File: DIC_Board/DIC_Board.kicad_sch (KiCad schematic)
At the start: 0 parts

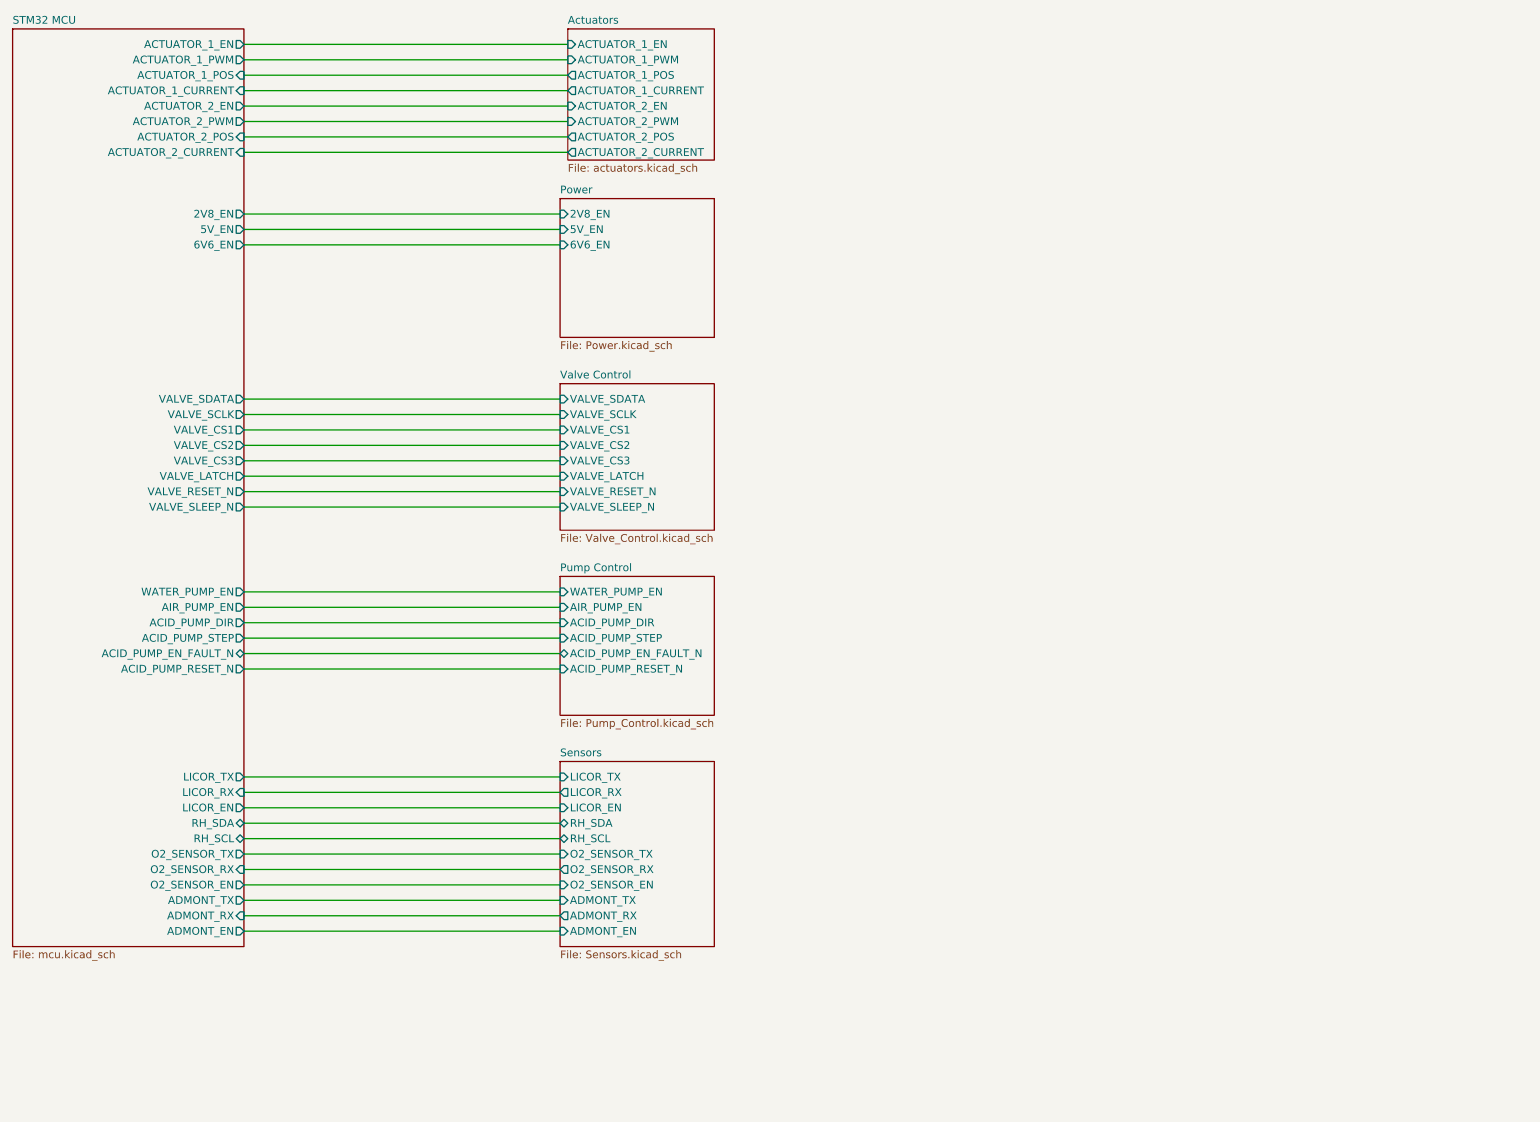
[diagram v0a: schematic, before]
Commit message: Synchronize power, communications, and MCU configuration
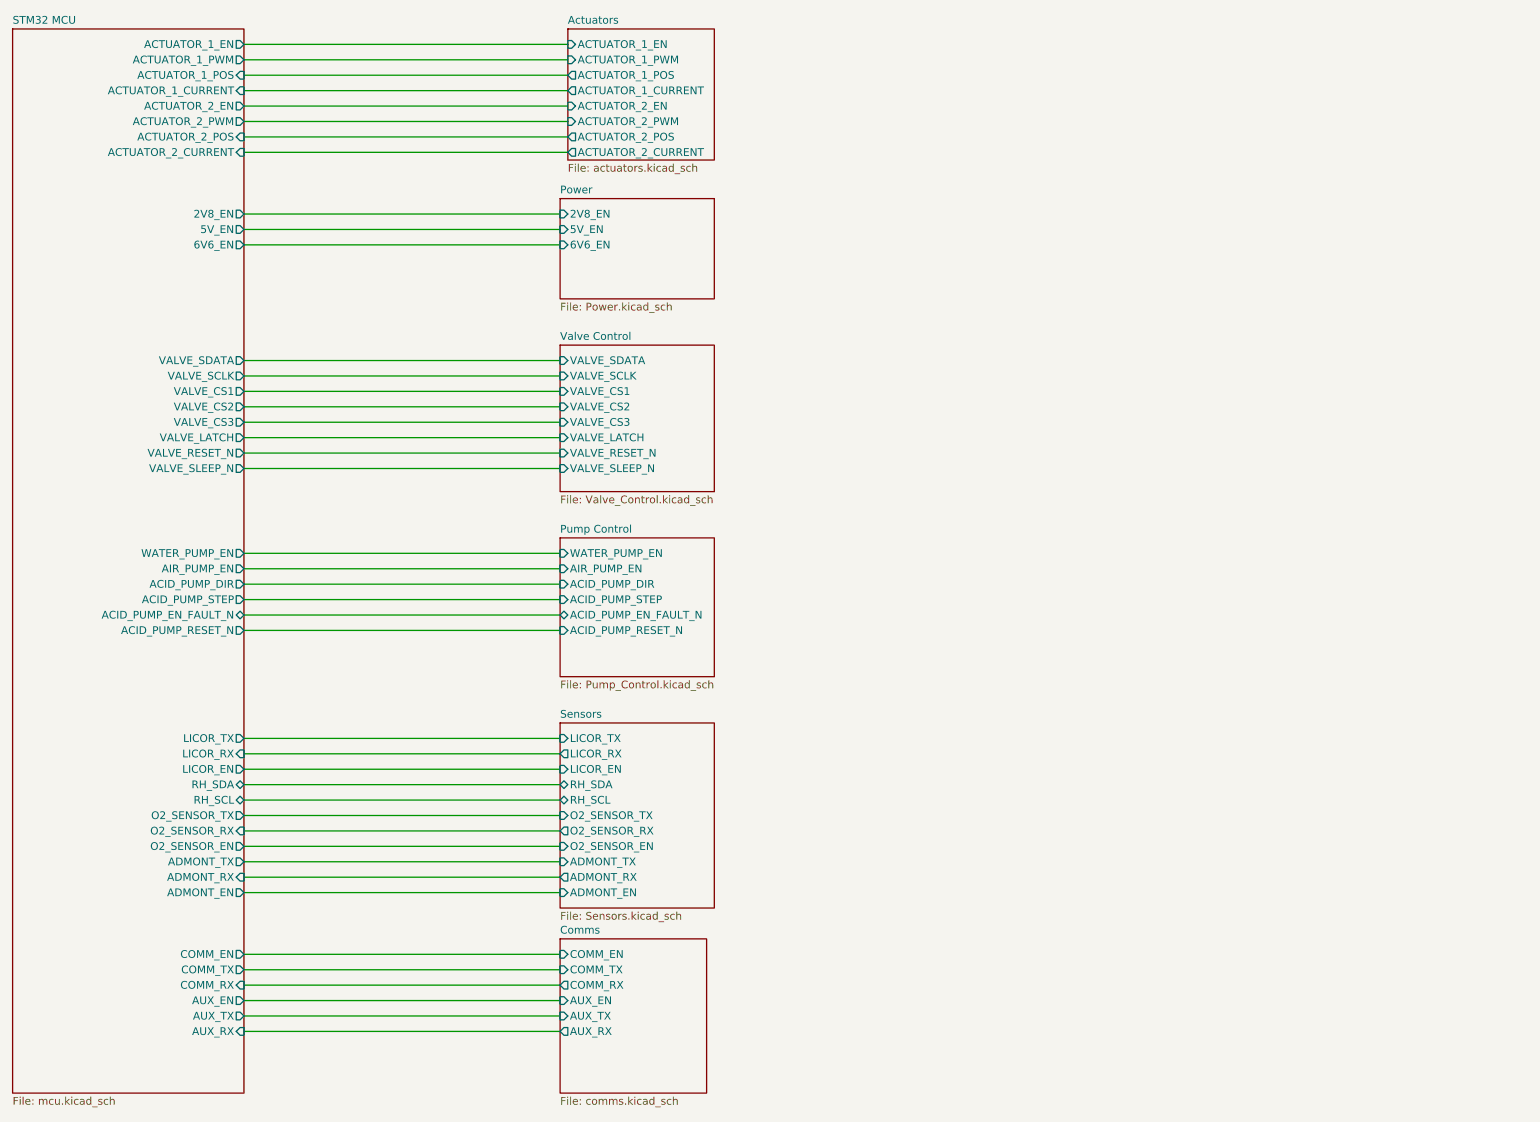
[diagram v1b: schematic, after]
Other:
- added sheet Comms (comms.kicad_sch)
- sheet STM32 MCU ports: added AUX_EN, AUX_RX, AUX_TX, COMM_EN, COMM_RX, COMM_TX; removed none

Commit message: Preliminary layout
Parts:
- added H1, H2, H3, H4: (no value), MountingHole:MountingHole_2.5mm_Pad, symbol Mechanical:MountingHole_Pad
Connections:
- new net GND: H1.1, H2.1, H3.1, H4.1
